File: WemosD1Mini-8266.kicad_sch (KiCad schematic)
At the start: 6 parts, among them J1 Conn_01x02_Pin, J2 Screw_Terminal_01x10, J3 Conn_01x02_Pin, U5 WeMos_D1_mini

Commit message: Version 1.1
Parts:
- removed J1: Conn_01x02_Pin, Connector_PinHeader_2.54mm:PinHeader_1x02_P2.54mm_Vertical, symbol Connector:Conn_01x02_Pin
- added H1: MountingHole, MountingHole:MountingHole_3.2mm_M3, symbol Mechanical:MountingHole
- added J2, J5, J6, J7: Conn_01x02_Pin, Connector_JST:JST_XH_B2B-XH-A_1x02_P2.50mm_Vertical, symbol Connector:Conn_01x02_Pin
- added J4: Conn_01x04_Pin, Connector_JST:JST_XH_B4B-XH-A_1x04_P2.50mm_Vertical, symbol Connector:Conn_01x04_Pin
- added J8: Screw_Terminal_01x08, TerminalBlock_Phoenix:TerminalBlock_Phoenix_MKDS-3-8-5.08_1x08_P5.08mm_Horizontal, symbol Connector:Screw_Terminal_01x08
- added R4: 2.2K, Resistor_SMD:R_0805_2012Metric_Pad1.20x1.40mm_HandSolder, symbol Device:R
- added R4: 0, Resistor_SMD:R_0805_2012Metric_Pad1.20x1.40mm_HandSolder, symbol Device:R
- added R4: 6.8K, Resistor_SMD:R_0805_2012Metric_Pad1.20x1.40mm_HandSolder, symbol Device:R
- added R4: 5.6K, Resistor_SMD:R_0805_2012Metric_Pad1.20x1.40mm_HandSolder, symbol Device:R
- added R4: 10K, Resistor_SMD:R_0805_2012Metric_Pad1.20x1.40mm_HandSolder, symbol Device:R
- added RV1: Varistor, Varistor:RV_Disc_D12mm_W7.1mm_P7.5mm, symbol Device:Varistor
- J3: footprint Connector_PinHeader_2.54mm:PinHeader_1x02_P2.54mm_Vertical -> Connector_JST:JST_XH_B2B-XH-A_1x02_P2.50mm_Vertical
- renumbered J2 to J1
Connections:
- net +5V: now also J2.1 (Pin_1)
- net AC/L: now also R4.2; no longer PS1.1 (AC/L)
- net AC/N: now also RV1.2
- net Earth: now also J3.2 (Pin_2), J2.2 (Pin_2), J4.4 (Pin_4), J5.2 (Pin_2), J7.2 (Pin_2), R4.2; no longer J3.1 (Pin_1)
- net Voltage Sensing/In1: now also J5.1 (Pin_1)
- net Voltage Sensing/In2: now also J4.3 (Pin_3)
- net Voltage Sensing/In3: now also J4.2 (Pin_2)
- net Voltage Sensing/In4: now also J4.1 (Pin_1)
- net at U5.2 (A0): now also R4.1, R4.1, R4.2, R4.2
- net Voltage Sensing/+Vs renamed +3.3V
- net +3.3V: now also J3.1 (Pin_1), J6.1 (Pin_1), R4.1; no longer J3.2 (Pin_2)
- new net: J8.1 (Pin_1), J8.5 (Pin_5)
- new net: J8.2 (Pin_2), J8.6 (Pin_6)
- new net: J8.3 (Pin_3), J8.7 (Pin_7)
- new net: J8.4 (Pin_4), J8.8 (Pin_8)
- new net: J6.2 (Pin_2), R4.1
- new net: J7.1 (Pin_1), R4.2
- new net AC/L(P): PS1.1 (AC/L), R4.1, RV1.1
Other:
- moved on the sheet: C2, J1, U5

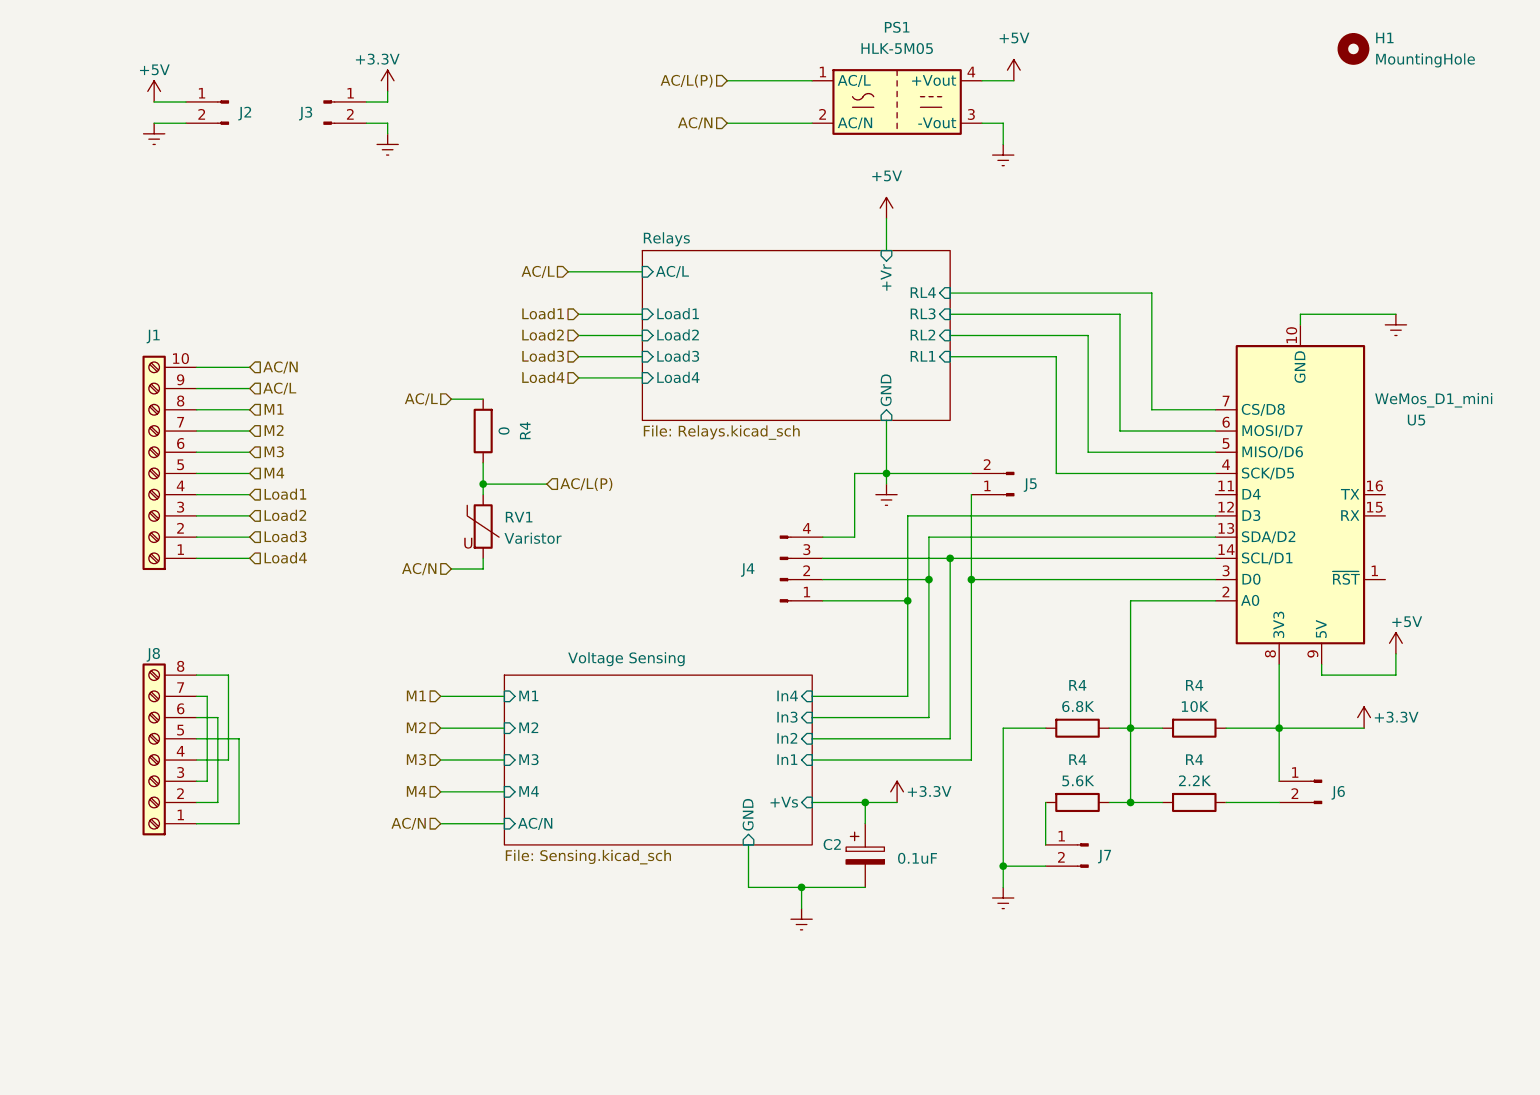
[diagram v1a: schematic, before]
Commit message: Version 1.2 Updates.
Added support for 3 digital switches via ADC.  Added MOV+Fuse protection
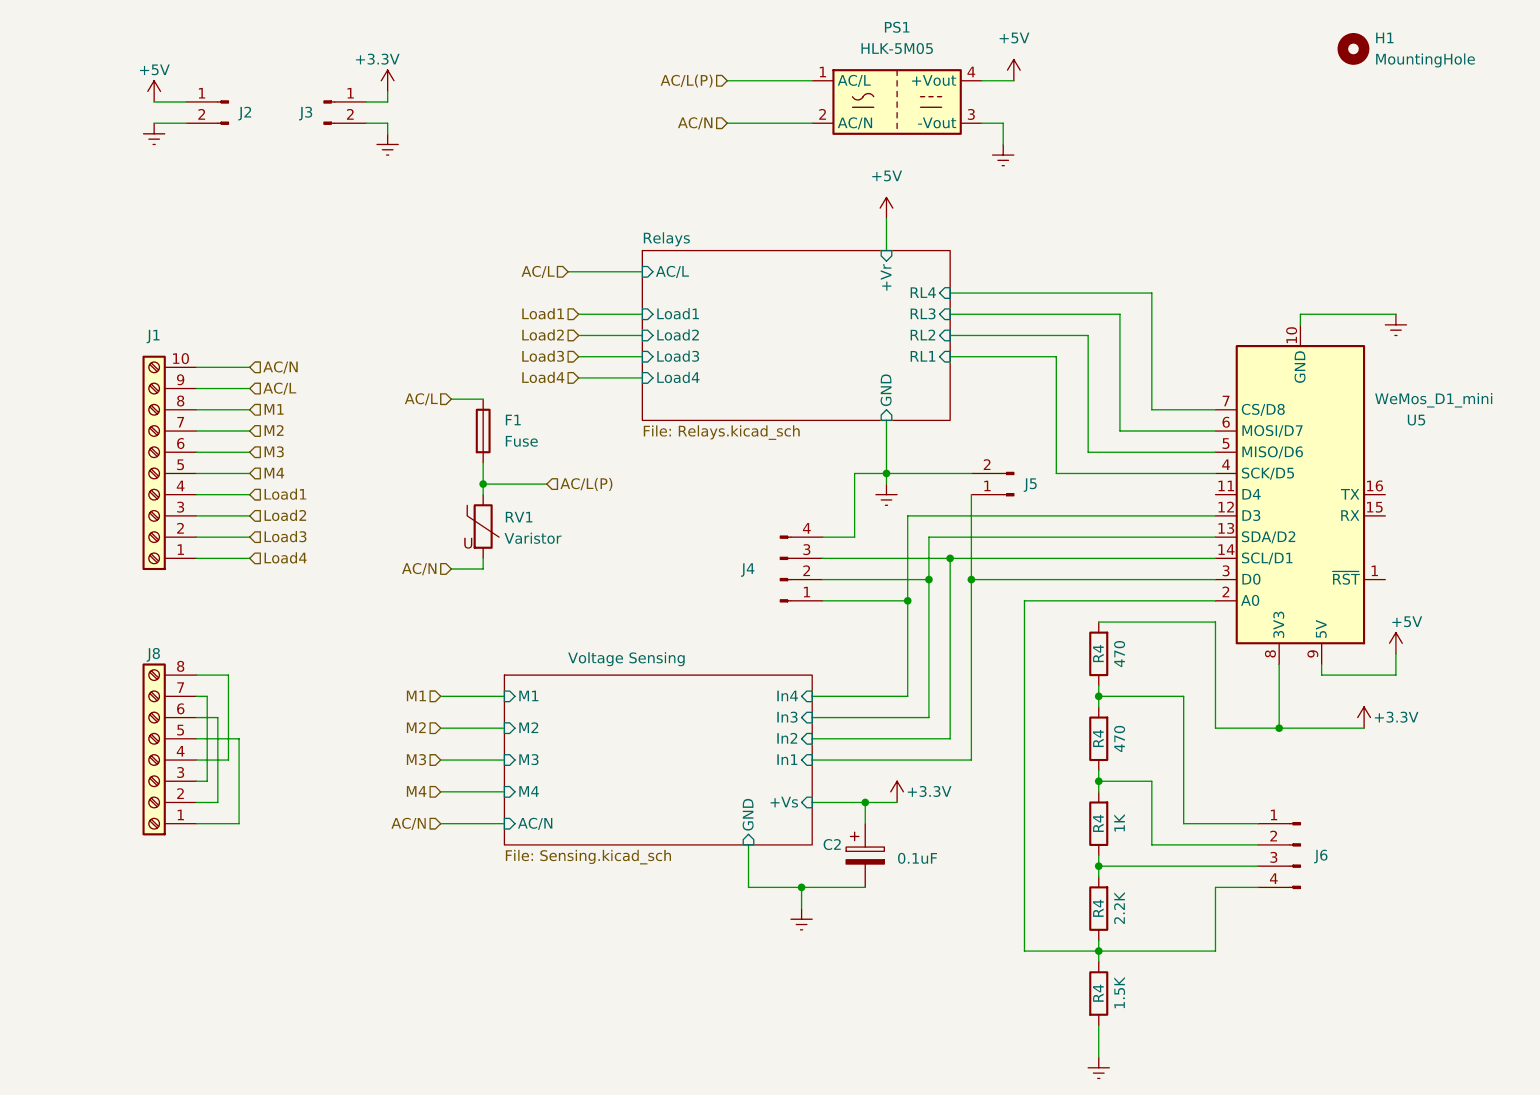
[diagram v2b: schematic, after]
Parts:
- removed J6, J7: Conn_01x02_Pin, Connector_JST:JST_XH_B2B-XH-A_1x02_P2.50mm_Vertical, symbol Connector:Conn_01x02_Pin
- added F1: Fuse, Fuse:Fuse_BelFuse_0ZRE0005FF_L8.3mm_W3.8mm, symbol Device:Fuse
- added J6: Conn_01x04_Pin, Connector_JST:JST_XH_B4B-XH-A_1x04_P2.50mm_Vertical, symbol Connector:Conn_01x04_Pin
- R4: value 2.2K -> 1K
- R4: value 0 -> 1.5K
- R4: value 6.8K -> 470
- R4: value 5.6K -> 2.2K
- R4: value 10K -> 470
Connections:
- net +3.3V: now also R4.2; no longer R4.1
- net AC/L: now also F1.1; no longer R4.2
- net AC/L(P): now also F1.2; no longer R4.1
- net Earth: now also R4.2; no longer R4.2
- net at R4.1: now also R4.2, J6.3 (Pin_3)
- new net: J6.1 (Pin_1), R4.1, R4.2
- new net: J6.2 (Pin_2), R4.1, R4.2
- new net: J6.4 (Pin_4), R4.1, R4.1, U5.2 (A0)
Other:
- moved on the sheet: R4

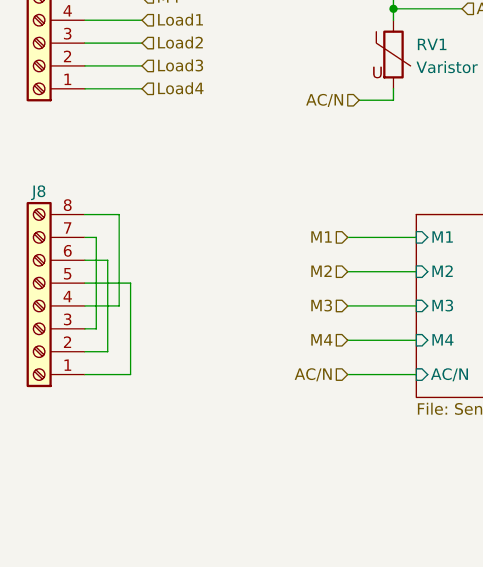
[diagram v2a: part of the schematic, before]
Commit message: V1.3 - Removed bypass PCB due to single design mandate from manufacturing.
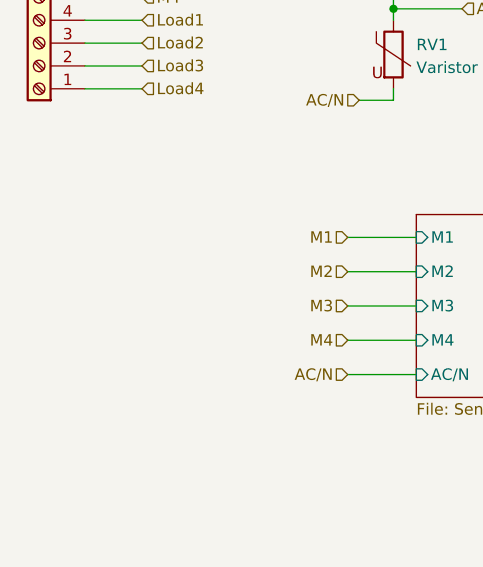
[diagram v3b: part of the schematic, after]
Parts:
- removed J8: Screw_Terminal_01x08, TerminalBlock_Phoenix:TerminalBlock_Phoenix_MKDS-3-8-5.08_1x08_P5.08mm_Horizontal, symbol Connector:Screw_Terminal_01x08
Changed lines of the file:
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@@
-    (stroke (width 0) (type default))
-  )
-  (wire (pts (xy 60.96 113.03) (xy 58.42 113.03))
     (stroke (width 0) (type default))
   )
@@
     (stroke (width 0) (type default))
   )
-  (wire (pts (xy 58.42 118.11) (xy 62.23 118.11))
-    (stroke (width 0) (type default))
-  )
-  (wire (pts (xy 59.69 120.65) (xy 59.69 110.49))
-    (stroke (width 0) (type default))
-  )
   (wire (pts (xy 180.34 93.98) (xy 148.59 93.98))
     (stroke (width 0) (type default))
@@
     (stroke (width 0) (type default))
   )
-  (wire (pts (xy 58.42 120.65) (xy 59.69 120.65))
-    (stroke (width 0) (type default))
-  )
   (wire (pts (xy 92.71 82.55) (xy 92.71 85.09))
     (stroke (width 0) (type default))
@@
     (stroke (width 0) (type default))
   )
-  (wire (pts (xy 63.5 125.73) (xy 63.5 115.57))
-    (stroke (width 0) (type default))
-  )
   (wire (pts (xy 152.4 36.83) (xy 156.21 36.83))
     (stroke (width 0) (type default))
@@
     (stroke (width 0) (type default))
   )
-  (wire (pts (xy 62.23 107.95) (xy 58.42 107.95))
-    (stroke (width 0) (type default))
-  )
   (wire (pts (xy 88.9 95.25) (xy 92.71 95.25))
     (stroke (width 0) (type default))
@@
     (stroke (width 0) (type default))
   )
-  (wire (pts (xy 59.69 110.49) (xy 58.42 110.49))
-    (stroke (width 0) (type default))
-  )
   (wire (pts (xy 81.28 39.37) (xy 78.74 39.37))
     (stroke (width 0) (type default))
@@
     (stroke (width 0) (type default))
   )
-  (wire (pts (xy 62.23 118.11) (xy 62.23 107.95))
-    (stroke (width 0) (type default))
-  )
   (wire (pts (xy 137.16 83.82) (xy 140.97 83.82))
     (stroke (width 0) (type default))
@@
     (stroke (width 0) (type default))
   )
-  (wire (pts (xy 58.42 125.73) (xy 63.5 125.73))
-    (stroke (width 0) (type default))
-  )
   (wire (pts (xy 104.14 67.31) (xy 111.76 67.31))
     (stroke (width 0) (type default))
   )
-  (wire (pts (xy 60.96 123.19) (xy 60.96 113.03))
-    (stroke (width 0) (type default))
-  )
   (wire (pts (xy 132.08 113.03) (xy 146.05 113.03))
     (stroke (width 0) (type default))
@@
     (stroke (width 0) (type default))
   )
-  (wire (pts (xy 63.5 115.57) (xy 58.42 115.57))
-    (stroke (width 0) (type default))
-  )
   (wire (pts (xy 87.63 125.73) (xy 95.25 125.73))
     (stroke (width 0) (type default))
@@
   )
   (wire (pts (xy 166.37 109.22) (xy 166.37 110.49))
-    (stroke (width 0) (type default))
-  )
-  (wire (pts (xy 58.42 123.19) (xy 60.96 123.19))
     (stroke (width 0) (type default))
   )
@@
         )
       )
-    )
-  )
-  (symbol (lib_id "Connector:Screw_Terminal_01x08") (at 53.34 118.11 180) (unit 1)
-    (in_bom yes) (on_board yes) (dnp no)
-    (property "Reference" "J8" (at 53.34 105.41 0)
-      (effects (font (size 1.27 1.27)))
-    )
-    (property "Value" "Screw_Terminal_01x08" (at 53.34 104.14 0)
-      (effects (font (size 1.27 1.27)) hide)
-    )
-    (property "Footprint" "TerminalBlock_Phoenix:TerminalBlock_Phoenix_MKDS-3-8-5.08_1x08_P5.08mm_Horizontal" (at 53.34 118.11 0)
-      (effects (font (size 1.27 1.27)) hide)
-    )
-    (property "Datasheet" "~" (at 53.34 118.11 0)
-      (effects (font (size 1.27 1.27)) hide)
-    )
-    (pin "1")
-    (pin "2")
-    (pin "3")
-    (pin "4")
-    (pin "5")
-    (pin "6")
-    (pin "7")
-    (pin "8")
-    (instances
-      (project "WemosD1Mini-8266"
-        (path "/84e8e68d-ec51-4c17-a8b1-603b22d1189f"
-          (reference "J8") (unit 1)
-        )
-      )
